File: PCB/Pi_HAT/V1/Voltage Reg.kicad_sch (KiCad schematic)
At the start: 7 parts, among them J4 Solenoid I2C, J5 XT60PW-M

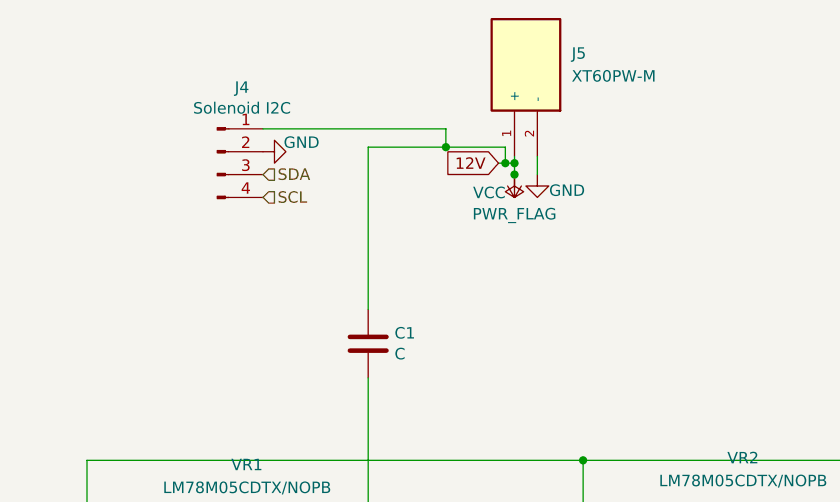
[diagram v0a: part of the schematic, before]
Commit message: Added Extra I2C Header
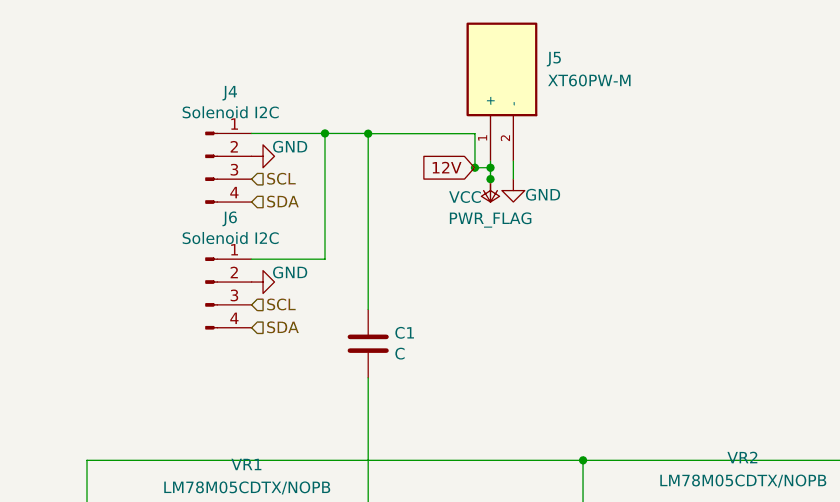
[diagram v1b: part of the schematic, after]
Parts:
- added J6: Solenoid I2C, Connector_PinHeader_2.54mm:PinHeader_1x04_P2.54mm_Vertical, symbol Connector:Conn_01x04_Male
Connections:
- net GND: now also J6.2 (Pin_2)
- net SCL: now also J4.3 (Pin_3), J6.3 (Pin_3); no longer J4.4 (Pin_4)
- net SDA: now also J4.4 (Pin_4), J6.4 (Pin_4); no longer J4.3 (Pin_3)
- net VCC: now also J6.1 (Pin_1)
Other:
- moved on the sheet: J4, J5

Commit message: Updated V1 Pi Hat
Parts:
- added J8: XT60PW-M, .pretty:AMASS_XT60PW-M, symbol XT60PW-M:XT60PW-M
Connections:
- net GND: now also J8.2 (-)
- net VCC: now also J8.1 (+)
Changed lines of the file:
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@@
     (stroke (width 0) (type default) (color 0 0 0 0))
+  )
+  (global_label "12V" (shape input) (at 143.51 45.72 270) (fields_autoplaced)
+    (effects (font (size 1.27 1.27)) (justify right))
+    (property "Intersheet References" "${INTERSHEET_REFS}" (id 0) (at 97.028 169.672 0)
+      (effects (font (size 1.27 1.27)) hide)
+    )
   )
   (global_label "12V" (shape input) (at 77.216 87.884 180) (fields_autoplaced)
@@
     (pin "1")
   )
+  (symbol (lib_id "power:GND") (at 146.05 45.72 0) (unit 1)
+    (in_bom yes) (on_board yes)
+    (property "Reference" "#PWR0113" (id 0) (at 146.05 52.07 0)
+      (effects (font (size 1.27 1.27)) hide)
+    )
+    (property "Value" "GND" (id 1) (at 149.352 47.498 0))
+    (property "Footprint" "" (id 2) (at 146.05 45.72 0)
+      (effects (font (size 1.27 1.27)) hide)
+    )
+    (property "Datasheet" "" (id 3) (at 146.05 45.72 0)
+      (effects (font (size 1.27 1.27)) hide)
+    )
+    (pin "1")
+  )
+  (symbol (lib_id "XT60PW-M:XT60PW-M") (at 146.05 35.56 90) (unit 1)
+    (in_bom yes) (on_board yes) (fields_autoplaced)
+    (property "Reference" "J8" (id 0) (at 149.86 34.2899 90)
+      (effects (font (size 1.27 1.27)) (justify right))
+    )
+    (property "Value" "XT60PW-M" (id 1) (at 149.86 36.8299 90)
+      (effects (font (size 1.27 1.27)) (justify right))
+    )
+    (property "Footprint" ".pretty:AMASS_XT60PW-M" (id 2) (at 146.05 35.56 0)
+      (effects (font (size 1.27 1.27)) (justify left bottom) hide)
+    )
+    (property "Datasheet" "" (id 3) (at 146.05 35.56 0)
+      (effects (font (size 1.27 1.27)) (justify left bottom) hide)
+    )
+    (property "STANDARD" "Manufacturer recommendations" (id 4) (at 146.05 35.56 0)
+      (effects (font (size 1.27 1.27)) (justify left bottom) hide)
+    )
+    (property "PARTREV" "V1.2" (id 5) (at 146.05 35.56 0)
+      (effects (font (size 1.27 1.27)) (justify left bottom) hide)
+    )
+    (property "MANUFACTURER" "AMASS" (id 6) (at 146.05 35.56 0)
+      (effects (font (size 1.27 1.27)) (justify left bottom) hide)
+    )
+    (property "MAXIMUM_PACKAGE_HEIGHT" "8.4 mm" (id 7) (at 146.05 35.56 0)
+      (effects (font (size 1.27 1.27)) (justify left bottom) hide)
+    )
+    (pin "1")
+    (pin "2")
+  )
   (symbol (lib_id "LM78M05CDTX_NOPB:LM78M05CDTX{slash}NOPB") (at 96.012 90.424 0) (unit 1)
